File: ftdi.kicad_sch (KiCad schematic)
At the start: 20 parts, among them U1 FT2232H-56Q

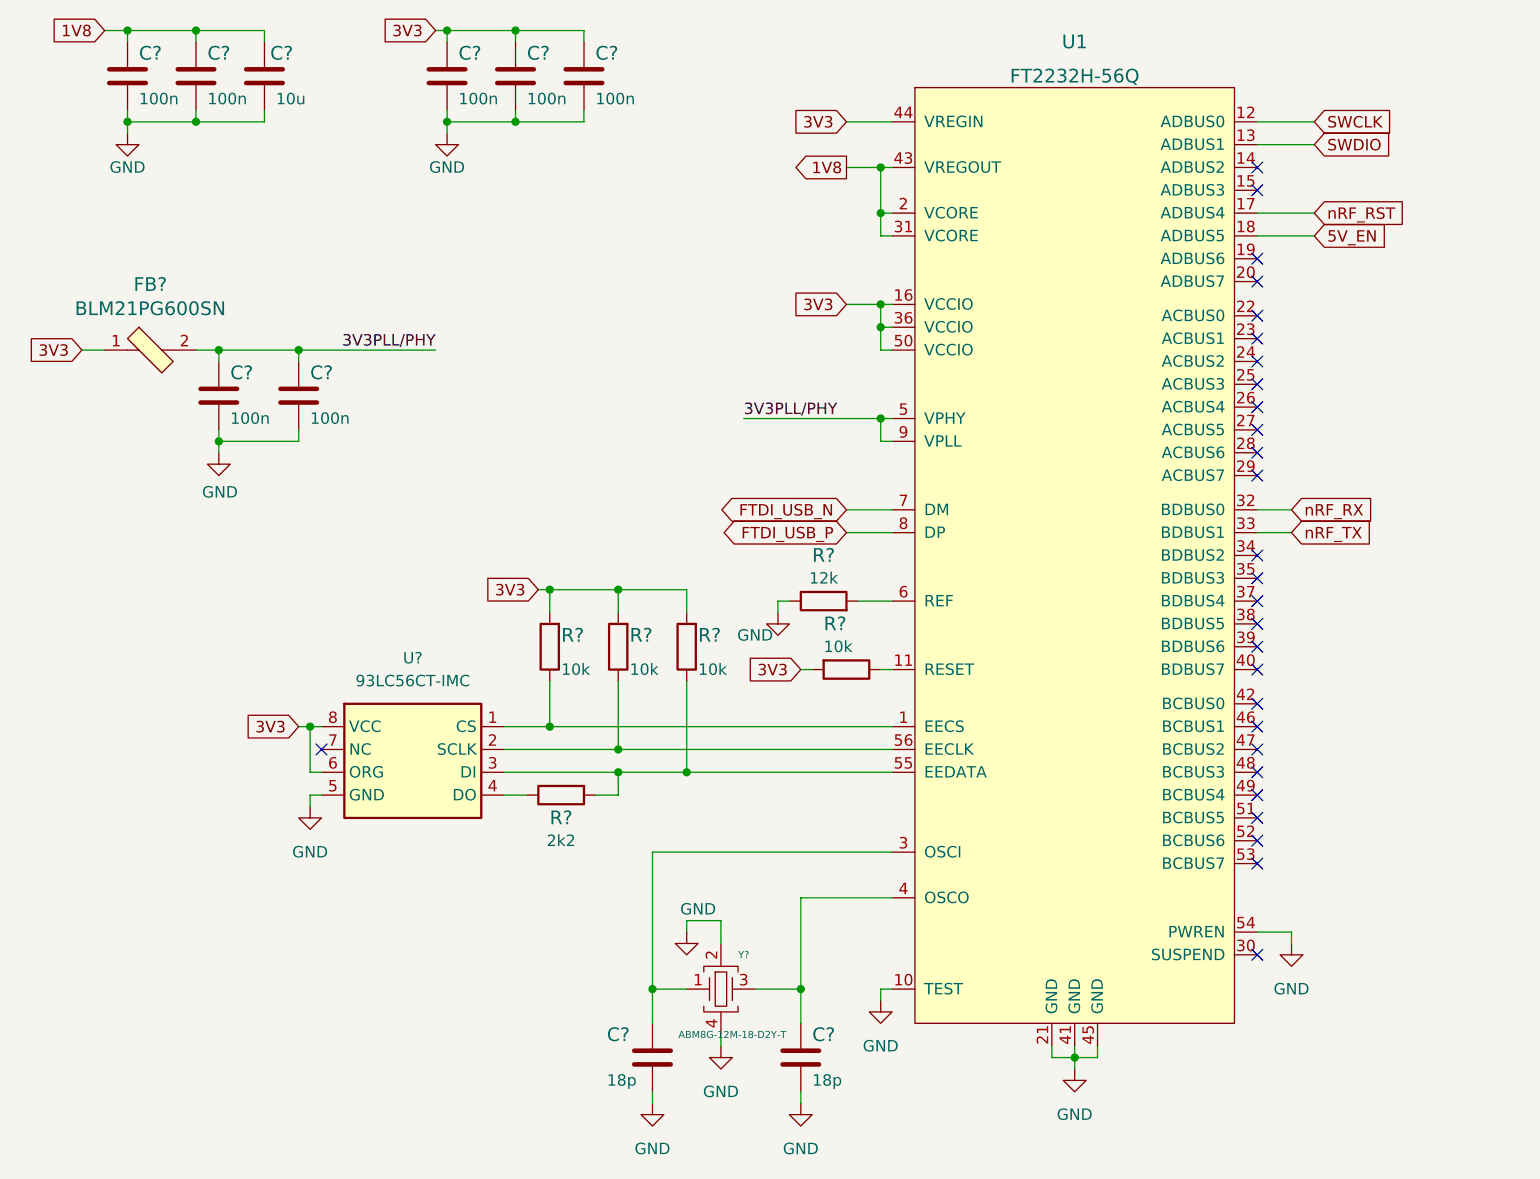
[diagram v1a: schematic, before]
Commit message: Created FT2232 layout
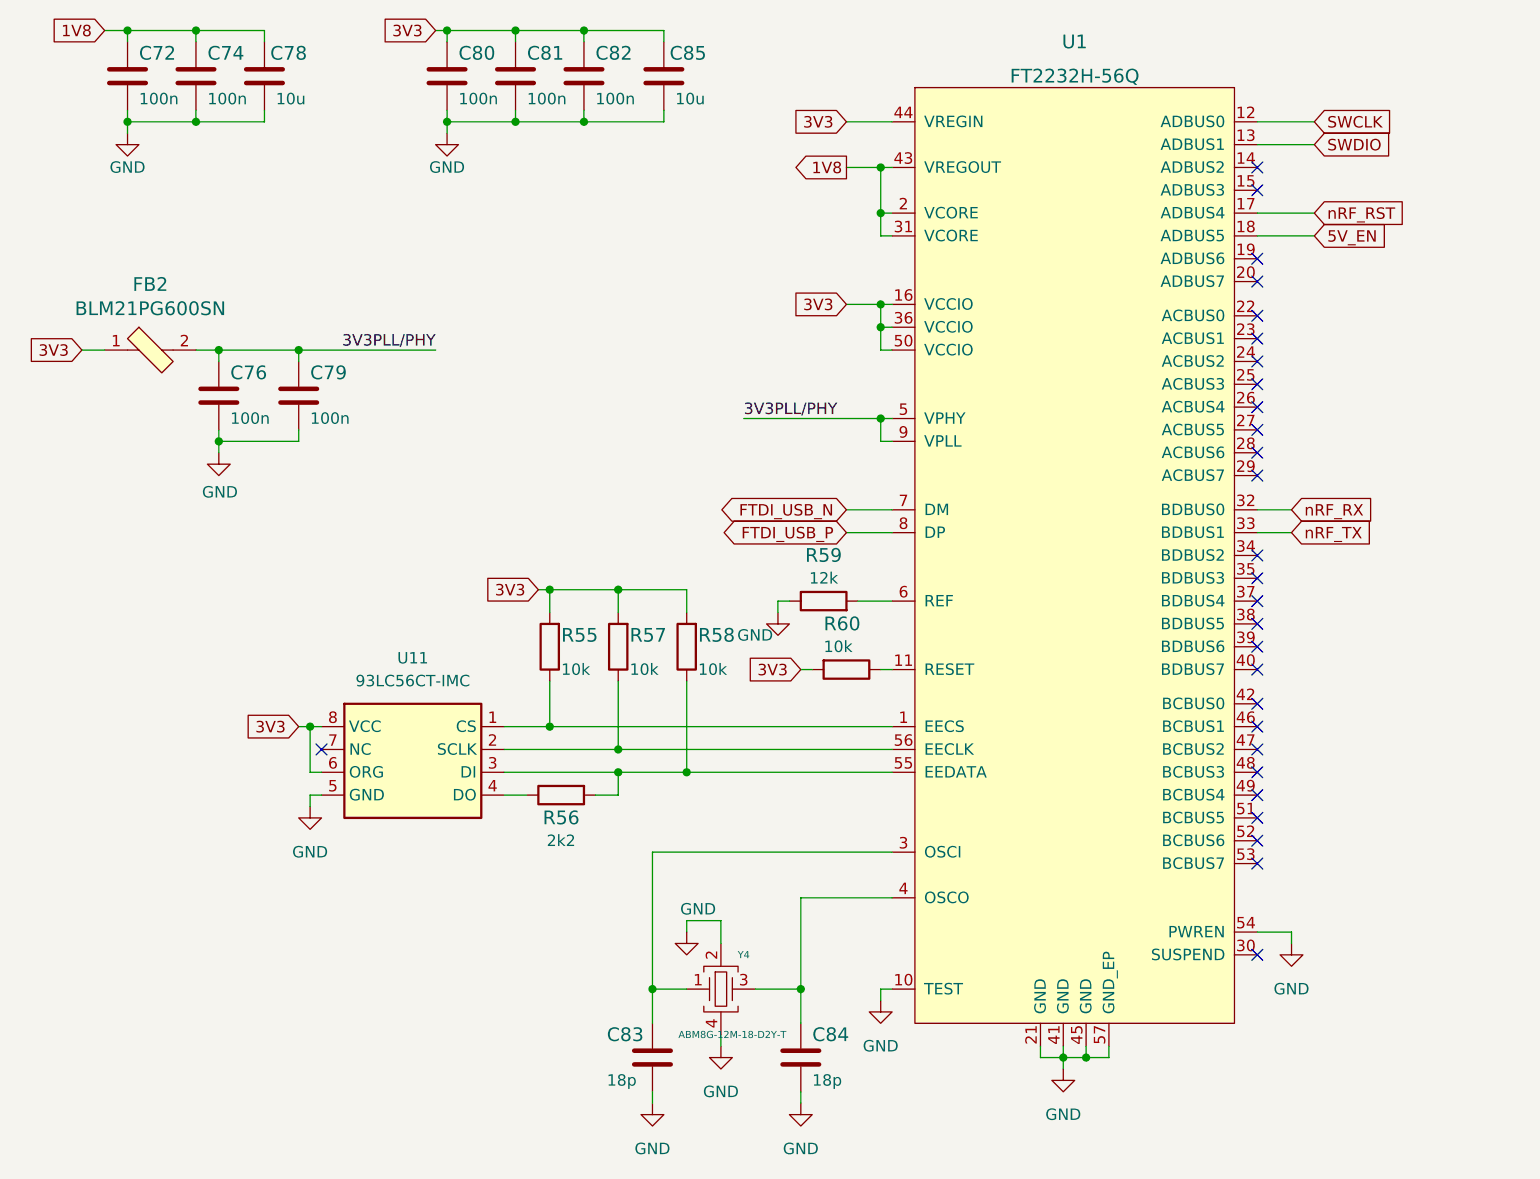
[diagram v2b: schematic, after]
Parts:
- added C85: C_10u_0805, m2-smart-iot-module-footprints:0805-cap, symbol m2-smart-iot-module:C_10u_0805
- gave numbers to parts that had none: 19
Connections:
- net 3V3: now also C85.1
- net GND: now also U1.57 (GND_EP), C85.2

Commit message: Layout touch-ups
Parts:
- added C?: C_100n_0402, antmicro-footprints:0402-cap, symbol antmicroCapacitors0402:C_100n_0402
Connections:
- net 3V3: now also C?.1
- net GND: now also C?.2
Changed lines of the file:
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@@
   (junction (at 58.42 109.22) (diameter 0) (color 0 0 0 0)
+  )
+  (junction (at 49.53 109.22) (diameter 0) (color 0 0 0 0)
   )
   (junction (at 121.92 74.93) (diameter 0) (color 0 0 0 0)
@@
     (stroke (width 0) (type default) (color 0 0 0 0))
   )
+  (wire (pts (xy 49.53 118.11) (xy 49.53 119.38))
+    (stroke (width 0) (type default) (color 0 0 0 0))
+  )
   (wire (pts (xy 38.1 40.64) (xy 38.1 41.91))
     (stroke (width 0) (type default) (color 0 0 0 0))
@@
     (stroke (width 0) (type default) (color 0 0 0 0))
   )
-  (wire (pts (xy 57.15 109.22) (xy 58.42 109.22))
+  (wire (pts (xy 48.26 109.22) (xy 49.53 109.22))
     (stroke (width 0) (type default) (color 0 0 0 0))
   )
@@
     (stroke (width 0) (type default) (color 0 0 0 0))
   )
+  (wire (pts (xy 49.53 109.22) (xy 49.53 110.49))
+    (stroke (width 0) (type default) (color 0 0 0 0))
+  )
   (wire (pts (xy 48.26 67.31) (xy 45.72 67.31))
     (stroke (width 0) (type default) (color 0 0 0 0))
@@
   )
   (wire (pts (xy 121.92 62.23) (xy 121.92 64.77))
+    (stroke (width 0) (type default) (color 0 0 0 0))
+  )
+  (wire (pts (xy 49.53 109.22) (xy 58.42 109.22))
     (stroke (width 0) (type default) (color 0 0 0 0))
   )
@@
     )
   )
-  (global_label "3V3" (shape input) (at 57.15 109.22 180) (fields_autoplaced)
+  (global_label "3V3" (shape input) (at 48.26 109.22 180) (fields_autoplaced)
     (effects (font (size 1.27 1.27)) (justify right))
-    (property "Intersheet References" "${INTERSHEET_REFS}" (id 0) (at -237.49 68.58 0)
+    (property "Intersheet References" "${INTERSHEET_REFS}" (id 0) (at -246.38 68.58 0)
       (effects (font (size 1.27 1.27)) hide)
     )
@@
     (pin "1")
   )
+  (symbol (lib_id "m2-smart-iot-module:GND") (at 49.53 119.38 0) (unit 1)
+    (in_bom yes) (on_board yes) (fields_autoplaced)
+    (property "Reference" "#PWR?" (id 0) (at 49.53 125.73 0)
+      (effects (font (size 1.27 1.27)) hide)
+    )
+    (property "Value" "GND" (id 1) (at 49.53 124.46 0))
+    (property "Footprint" "" (id 2) (at 49.53 119.38 0)
+      (effects (font (size 1.27 1.27)) hide)
+    )
+    (property "Datasheet" "" (id 3) (at 49.53 119.38 0)
+      (effects (font (size 1.27 1.27)) hide)
+    )
+    (pin "1")
+  )
   (symbol (lib_id "antmicroCapacitors0402:C_18p_0402") (at 113.03 146.05 0) (unit 1)
     (in_bom yes) (on_board yes)
@@
     (pin "1")
     (pin "2")
+  )
+  (symbol (lib_id "antmicroCapacitors0402:C_100n_0402") (at 49.53 114.3 0) (unit 1)
+    (in_bom yes) (on_board yes)
+    (property "Reference" "C?" (id 0) (at 50.8 111.76 0)
+      (effects (font (size 1.524 1.524)) (justify left))
+    )
+    (property "Value" "C_100n_0402" (id 1) (at 49.53 118.11 0)
+      (effects (font (size 1.524 1.524)) hide)
+    )
+    (property "Footprint" "antmicro-footprints:0402-cap" (id 2) (at 54.61 109.22 0)
+      (effects (font (size 1.524 1.524)) (justify left) hide)
+    )
+    (property "Datasheet" "" (id 3) (at 49.53 114.3 0)
+      (effects (font (size 1.27 1.27)) hide)
+    )
+    (property "Manufacturer" "Murata" (id 4) (at 54.61 104.14 0)
+      (effects (font (size 1.524 1.524)) (justify left) hide)
+    )
+    (property "MPN" "GRM155R61H104KE14D" (id 5) (at 54.61 106.68 0)
+      (effects (font (size 1.524 1.524)) (justify left) hide)
+    )
+    (property "Val" "100n" (id 6) (at 50.8 116.84 0)
+      (effects (font (size 1.27 1.27)) (justify left))
+    )
+    (pin "1")
+    (pin "2")

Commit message: Bumped version to 1.2.2
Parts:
- gave numbers to parts that had none: 1
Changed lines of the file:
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@@
   (title_block
     (date "2022-07-11")
-    (rev "1.2.1")
+    (rev "1.2.2")
   )
   (junction (at 73.66 31.75) (diameter 0) (color 0 0 0 0)
@@
   (symbol (lib_id "m2-smart-iot-module:GND") (at 49.53 119.38 0) (unit 1)
     (in_bom yes) (on_board yes) (fields_autoplaced)
-    (property "Reference" "#PWR?" (id 0) (at 49.53 125.73 0)
+    (property "Reference" "#PWR0121" (id 0) (at 49.53 125.73 0)
       (effects (font (size 1.27 1.27)) hide)
     )
@@
   (symbol (lib_id "antmicroCapacitors0402:C_100n_0402") (at 49.53 114.3 0) (unit 1)
     (in_bom yes) (on_board yes)
-    (property "Reference" "C?" (id 0) (at 50.8 111.76 0)
+    (property "Reference" "C86" (id 0) (at 50.8 111.76 0)
       (effects (font (size 1.524 1.524)) (justify left))
     )

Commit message: Fixed SWD
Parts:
- added R61: R_470R_0402, antmicro-footprints:0402-res, symbol antmicroResistors0402:R_470R_0402
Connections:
- net SWDIO: now also R61.2
- net at U1.14 (ADBUS2): now also R61.1
- no-connect marks 28 -> 27
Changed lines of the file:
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@@
   (junction (at 45.72 31.75) (diameter 0) (color 0 0 0 0)
+  )
+  (junction (at 176.53 44.45) (diameter 0) (color 0 0 0 0)
   )
   (junction (at 38.1 41.91) (diameter 0) (color 0 0 0 0)
@@
   (no_connect (at 163.83 97.79))
   (no_connect (at 163.83 124.46))
-  (no_connect (at 163.83 46.99))
   (no_connect (at 163.83 49.53))
   (no_connect (at 163.83 57.15))
@@
     (stroke (width 0) (type default) (color 0 0 0 0))
   )
+  (wire (pts (xy 176.53 44.45) (xy 182.88 44.45))
+    (stroke (width 0) (type default) (color 0 0 0 0))
+  )
   (wire (pts (xy 85.09 93.98) (xy 92.71 93.98))
     (stroke (width 0) (type default) (color 0 0 0 0))
@@
     (stroke (width 0) (type default) (color 0 0 0 0))
   )
-  (wire (pts (xy 163.83 44.45) (xy 170.18 44.45))
+  (wire (pts (xy 163.83 44.45) (xy 176.53 44.45))
     (stroke (width 0) (type default) (color 0 0 0 0))
   )
@@
     (stroke (width 0) (type default) (color 0 0 0 0))
   )
+  (wire (pts (xy 176.53 46.99) (xy 176.53 44.45))
+    (stroke (width 0) (type default) (color 0 0 0 0))
+  )
   (wire (pts (xy 73.66 31.75) (xy 81.28 31.75))
     (stroke (width 0) (type default) (color 0 0 0 0))
@@
     (stroke (width 0) (type default) (color 0 0 0 0))
   )
+  (wire (pts (xy 163.83 46.99) (xy 166.37 46.99))
+    (stroke (width 0) (type default) (color 0 0 0 0))
+  )
   (wire (pts (xy 81.28 41.91) (xy 88.9 41.91))
     (stroke (width 0) (type default) (color 0 0 0 0))
@@
   )
   (wire (pts (xy 83.82 93.98) (xy 85.09 93.98))
+    (stroke (width 0) (type default) (color 0 0 0 0))
+  )
+  (wire (pts (xy 173.99 46.99) (xy 176.53 46.99))
     (stroke (width 0) (type default) (color 0 0 0 0))
   )
@@
     )
   )
-  (global_label "SWDIO" (shape input) (at 170.18 44.45 0) (fields_autoplaced)
+  (global_label "SWDIO" (shape input) (at 182.88 44.45 0) (fields_autoplaced)
     (effects (font (size 1.27 1.27)) (justify left))
-    (property "Intersheet References" "${INTERSHEET_REFS}" (id 0) (at 178.3704 44.3706 0)
+    (property "Intersheet References" "${INTERSHEET_REFS}" (id 0) (at 191.0704 44.3706 0)
       (effects (font (size 1.27 1.27)) (justify left) hide)
     )
@@
     (pin "1")
   )
+  (symbol (lib_id "antmicroResistors0402:R_470R_0402") (at 170.18 46.99 0) (unit 1)
+    (in_bom yes) (on_board yes)
+    (property "Reference" "R61" (id 0) (at 173.99 49.53 0)
+      (effects (font (size 1.524 1.524)))
+    )
+    (property "Value" "R_470R_0402" (id 1) (at 170.18 50.8 0)
+      (effects (font (size 1.524 1.524)) hide)
+    )
+    (property "Footprint" "antmicro-footprints:0402-res" (id 2) (at 175.26 41.91 0)
+      (effects (font (size 1.524 1.524)) (justify left) hide)
+    )
+    (property "Datasheet" "" (id 3) (at 170.18 46.99 0)
+      (effects (font (size 1.27 1.27)) hide)
+    )
+    (property "Manufacturer" "VISHAY" (id 4) (at 175.26 36.83 0)
+      (effects (font (size 1.524 1.524)) (justify left) hide)
+    )
+    (property "MPN" "CRCW0402470RFKED" (id 5) (at 175.26 39.37 0)
+      (effects (font (size 1.524 1.524)) (justify left) hide)
+    )
+    (property "Val" "470R" (id 6) (at 168.91 49.53 0))
+    (pin "1")
+    (pin "2")
+  )
   (symbol (lib_id "antmicroMemory:93LC56CT-IMC") (at 69.85 111.76 0) (unit 1)

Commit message: Applied fixes to issues that came up in review
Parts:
- added C87: C_10u_0603, antmicro-footprints:0603-cap, symbol antmicroCapacitors0603:C_10u_0603
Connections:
- net 3V3PLL/PHY: now also C87.1
- net GND: now also C87.2
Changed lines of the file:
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@@
   (junction (at 38.1 31.75) (diameter 0) (color 0 0 0 0)
   )
+  (junction (at 66.04 67.31) (diameter 0) (color 0 0 0 0)
+  )
   (junction (at 45.72 31.75) (diameter 0) (color 0 0 0 0)
   )
@@
   )
   (junction (at 121.92 46.99) (diameter 0) (color 0 0 0 0)
+  )
+  (junction (at 57.15 77.47) (diameter 0) (color 0 0 0 0)
   )
   (no_connect (at 163.83 119.38))
@@
     (stroke (width 0) (type default) (color 0 0 0 0))
   )
+  (wire (pts (xy 66.04 76.2) (xy 66.04 77.47))
+    (stroke (width 0) (type default) (color 0 0 0 0))
+  )
   (wire (pts (xy 167.64 133.35) (xy 167.64 132.08))
     (stroke (width 0) (type default) (color 0 0 0 0))
@@
     (stroke (width 0) (type default) (color 0 0 0 0))
   )
-  (wire (pts (xy 57.15 67.31) (xy 72.39 67.31))
+  (wire (pts (xy 66.04 67.31) (xy 66.04 68.58))
+    (stroke (width 0) (type default) (color 0 0 0 0))
+  )
+  (wire (pts (xy 57.15 67.31) (xy 66.04 67.31))
     (stroke (width 0) (type default) (color 0 0 0 0))
   )
@@
     (stroke (width 0) (type default) (color 0 0 0 0))
   )
+  (wire (pts (xy 66.04 77.47) (xy 57.15 77.47))
+    (stroke (width 0) (type default) (color 0 0 0 0))
+  )
   (wire (pts (xy 106.68 74.93) (xy 121.92 74.93))
     (stroke (width 0) (type default) (color 0 0 0 0))
@@
     (stroke (width 0) (type default) (color 0 0 0 0))
   )
+  (wire (pts (xy 66.04 67.31) (xy 82.55 67.31))
+    (stroke (width 0) (type default) (color 0 0 0 0))
+  )
   (wire (pts (xy 173.99 46.99) (xy 176.53 46.99))
     (stroke (width 0) (type default) (color 0 0 0 0))
@@
     (stroke (width 0) (type default) (color 0 0 0 0))
   )
-  (label "3V3PLL{slash}PHY" (at 72.39 67.31 180)
+  (label "3V3PLL{slash}PHY" (at 82.55 67.31 180)
     (effects (font (size 1.27 1.27)) (justify right bottom))
   )
@@
       (effects (font (size 1.27 1.27)) (justify left))
     )
+    (pin "1")
+    (pin "2")
+  )
+  (symbol (lib_id "antmicroCapacitors0603:C_10u_0603") (at 66.04 72.39 0) (unit 1)
+    (in_bom yes) (on_board yes) (fields_autoplaced)
+    (property "Reference" "C87" (id 0) (at 69.85 71.12 0)
+      (effects (font (size 1.524 1.524)) (justify left))
+    )
+    (property "Value" "C_10u_0603" (id 1) (at 66.04 76.2 0)
+      (effects (font (size 1.524 1.524)) hide)
+    )
+    (property "Footprint" "antmicro-footprints:0603-cap" (id 2) (at 71.12 67.31 0)
+      (effects (font (size 1.524 1.524)) (justify left) hide)
+    )
+    (property "Datasheet" "" (id 3) (at 66.04 72.39 0)
+      (effects (font (size 1.27 1.27)) hide)
+    )
+    (property "Manufacturer" "Murata" (id 4) (at 71.12 62.23 0)
+      (effects (font (size 1.524 1.524)) (justify left) hide)
+    )
+    (property "MPN" "GRM188R61A106KE69D" (id 5) (at 71.12 64.77 0)
+      (effects (font (size 1.524 1.524)) (justify left) hide)
+    )
+    (property "Val" "10u" (id 6) (at 69.85 74.2949 0)
+      (effects (font (size 1.27 1.27)) (justify left))
+    )
